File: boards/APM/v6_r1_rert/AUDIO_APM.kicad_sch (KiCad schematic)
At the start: 3 parts, among them J11 DAC_L_PRB, J12 Conn_01x02, J7 DAC_R_PRB

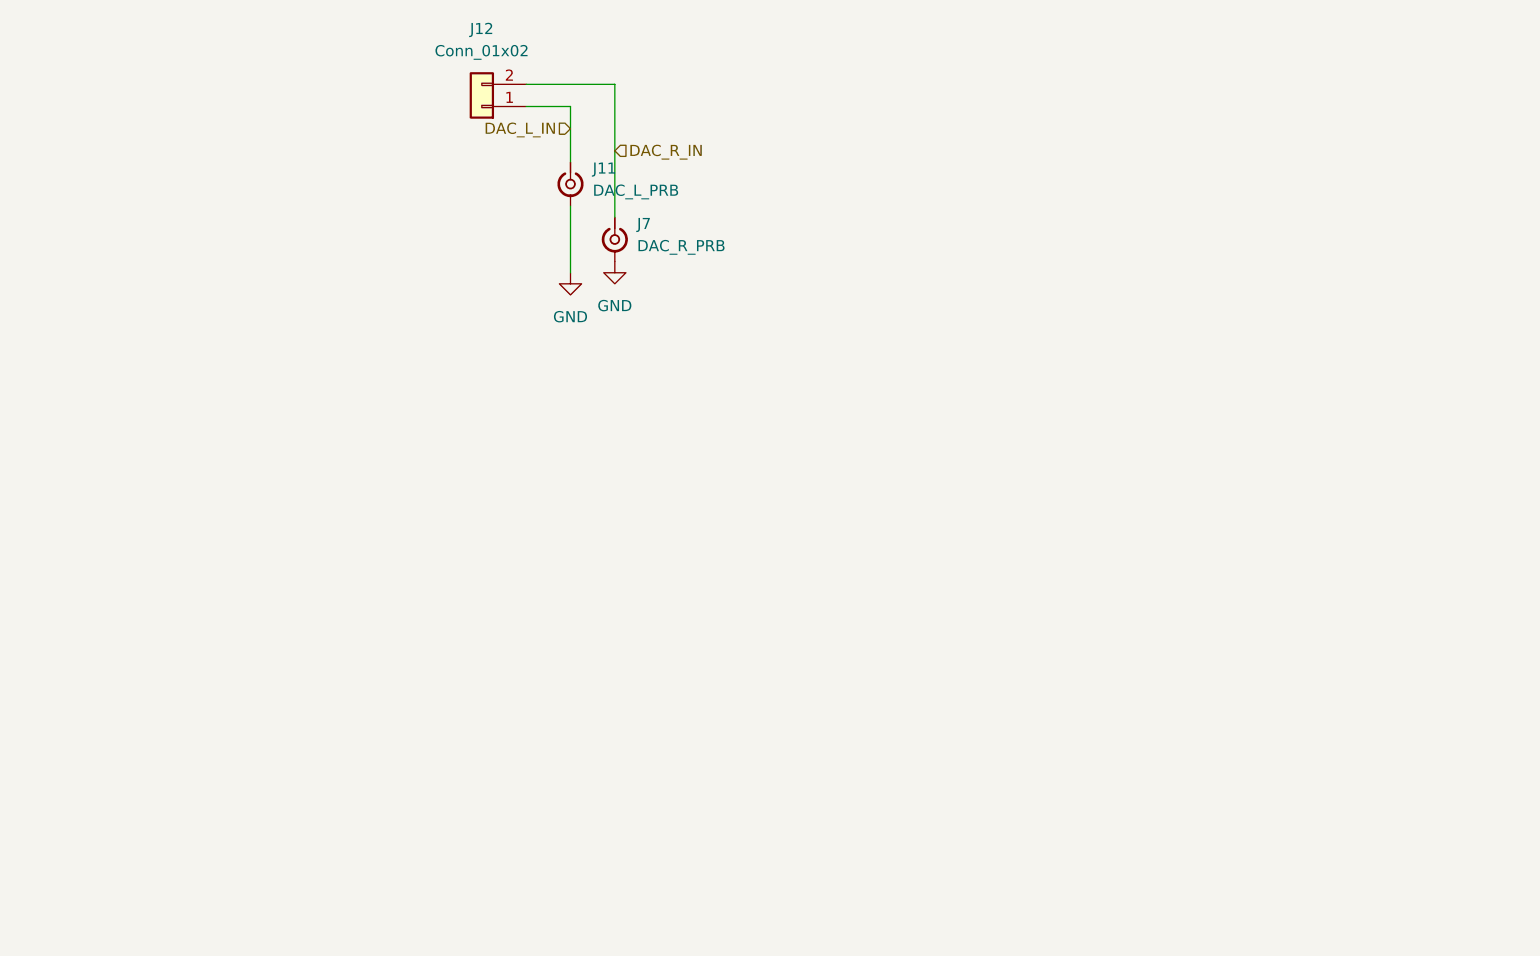
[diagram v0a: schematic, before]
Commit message: new APM rerouted looks better, passes DRC...
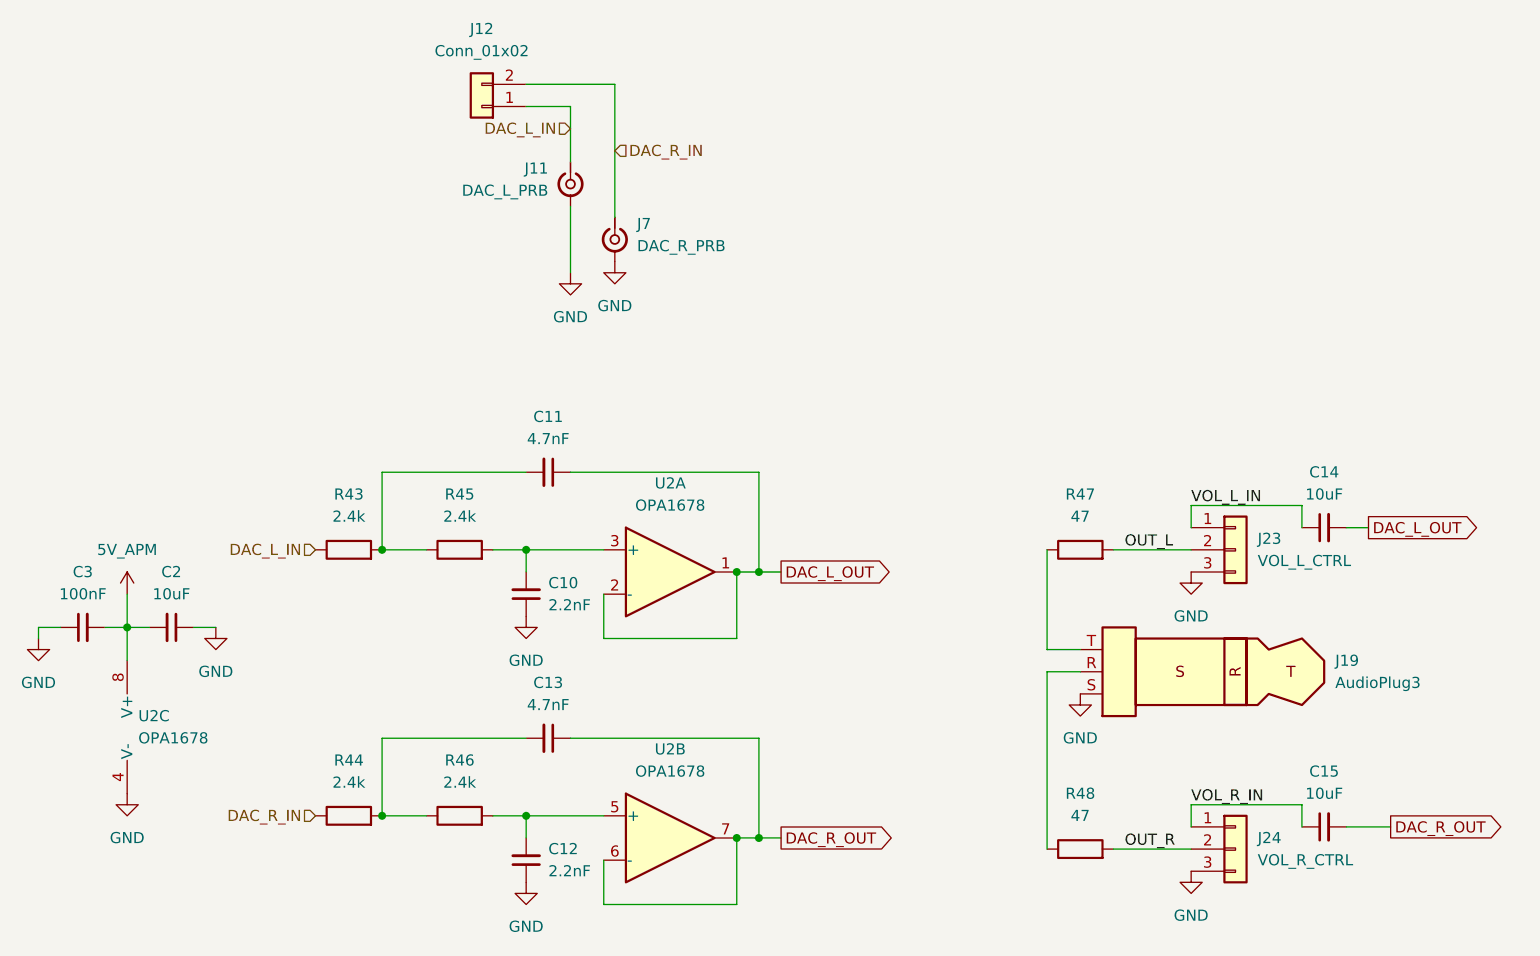
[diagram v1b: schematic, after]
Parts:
- added C10, C12: 2.2nF, Capacitor_SMD:C_0805_2012Metric, symbol Device:C_Small
- added C11, C13: 4.7nF, Capacitor_SMD:C_0805_2012Metric, symbol Device:C_Small
- added C14, C15, C2: 10uF, Capacitor_SMD:CP_Elec_4x3, symbol Device:C_Small
- added C3: 100nF, Capacitor_SMD:C_0805_2012Metric, symbol Device:C_Small
- added J19: AudioPlug3, Connector_Audio:Jack_3.5mm_Ledino_KB3SPRS_Horizontal, symbol Connector_Audio:AudioPlug3
- added J23: VOL_L_CTRL, Connector_PinHeader_2.54mm:PinHeader_1x03_P2.54mm_Vertical, symbol Connector_Generic:Conn_01x03
- added J24: VOL_R_CTRL, Connector_PinHeader_2.54mm:PinHeader_1x03_P2.54mm_Vertical, symbol Connector_Generic:Conn_01x03
- added R43, R44, R45, R46: 2.4k, Resistor_SMD:R_0201_0603Metric, symbol Device:R
- added R47, R48: 47, Resistor_SMD:R_0201_0603Metric, symbol Device:R
- added U2: OPA1678, Package_DIP:DIP-8_W7.62mm_SMDSocket_SmallPads, symbol Amplifier_Operational:OPA1678
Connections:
- net DAC_L_IN: now also R43.1
- net DAC_R_IN: now also R44.1
- net GND: now also C10.1, C12.1, C2.1, C3.1, J19.S, J23.3 (Pin_3), J24.3 (Pin_3), U2.4 (V-)
- new net: C10.2, R45.2, U2.3 (+)
- new net: C11.2, R43.2, R45.1
- new net: C13.2, R44.2, R46.1
- new net: J19.R, R48.1
- new net: J19.T, R47.1
- new net: C12.2, R46.2, U2.5 (+)
- new net 5V_APM: C2.2, C3.2, U2.8 (V+)
- new net DAC_L_OUT: C11.1, C14.2, U2.1, U2.2 (-)
- new net DAC_R_OUT: C13.1, C15.2, U2.6 (-), U2.7
- new net OUT_L: J23.2 (Pin_2), R47.2
- new net OUT_R: J24.2 (Pin_2), R48.2
- new net VOL_L_IN: C14.1, J23.1 (Pin_1)
- new net VOL_R_IN: C15.1, J24.1 (Pin_1)
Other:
- moved on the sheet: J11

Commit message: hmmm if i'm creating a minimal combination board maybe i don't blow up routing right now...
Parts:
- removed C10, C12: 2.2nF, Capacitor_SMD:C_0805_2012Metric, symbol Device:C_Small
- removed C11, C13: 4.7nF, Capacitor_SMD:C_0805_2012Metric, symbol Device:C_Small
- removed C14, C15, C2: 10uF, Capacitor_SMD:CP_Elec_4x3, symbol Device:C_Small
- removed C3: 100nF, Capacitor_SMD:C_0805_2012Metric, symbol Device:C_Small
- removed J19: AudioPlug3, Connector_Audio:Jack_3.5mm_Ledino_KB3SPRS_Horizontal, symbol Connector_Audio:AudioPlug3
- removed J23: VOL_L_CTRL, Connector_PinHeader_2.54mm:PinHeader_1x03_P2.54mm_Vertical, symbol Connector_Generic:Conn_01x03
- removed J24: VOL_R_CTRL, Connector_PinHeader_2.54mm:PinHeader_1x03_P2.54mm_Vertical, symbol Connector_Generic:Conn_01x03
- removed R43, R44, R45, R46: 2.4k, Resistor_SMD:R_0201_0603Metric, symbol Device:R
- removed R47, R48: 47, Resistor_SMD:R_0201_0603Metric, symbol Device:R
- removed U2: OPA1678, Package_DIP:DIP-8_W7.62mm_SMDSocket_SmallPads, symbol Amplifier_Operational:OPA1678
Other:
- moved on the sheet: J11
